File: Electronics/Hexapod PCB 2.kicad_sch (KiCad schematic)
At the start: 68 parts, among them J1 XT60, J2 leg1, J3 leg2, J4 leg3, J5 leg4, J6 leg5, J7 leg6, J8 USB_C_Receptacle_USB2.0_16P, Q1 IRF4905, Q2 Q_NPN_BCE, Q3 Q_NPN_BCE, SW1 SW_SPST, SW2 SW_SPST, SW3 SW_SPST, U1 TPS563201, U2 TPS563201, U3 ESP32-S3-WROOM-1, U4 USBLC6-2P6, U5 BNO055, U6 INA226

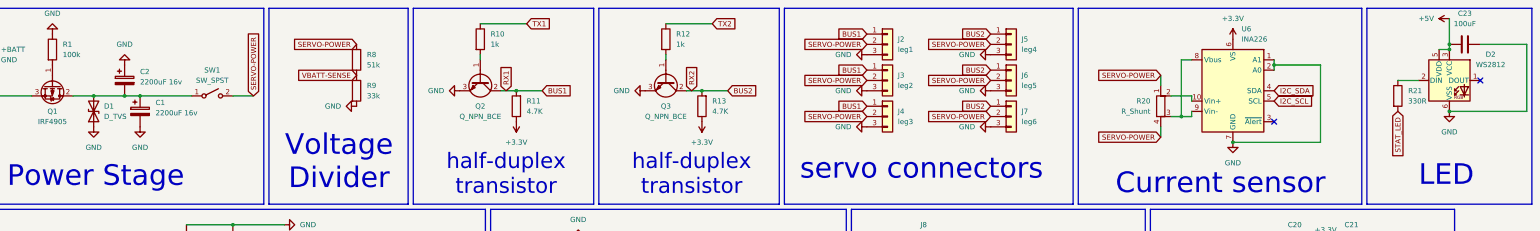
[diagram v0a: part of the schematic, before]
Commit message: finished the schmeatics by redesigning the INA226 , set all of the footprint for the schematics
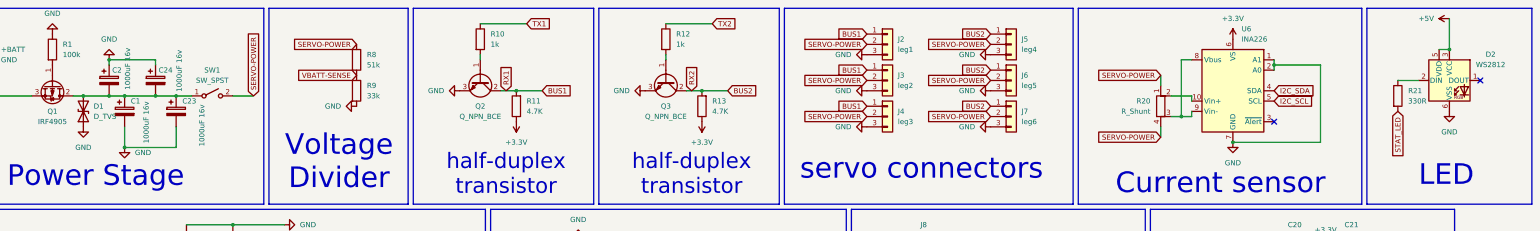
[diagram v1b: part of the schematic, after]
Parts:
- removed C23: 100uF, symbol Device:C
- added C23, C24: 1000uF 16v, Capacitor_SMD:CP_Elec_10x10, symbol Device:C_Polarized
- C1, C2: value 2200uF 16v -> 1000uF 16v; footprint (none) -> Capacitor_SMD:CP_Elec_10x10
- C10, C11, C12, C13, C14, C15, C16, C17, C18, C19, C20, C21, C22, C3, C4, C5, C6, C7, C8, C9: footprint (none) -> Capacitor_SMD:C_0805_2012Metric
- D1: footprint (none) -> Diode_SMD:D_SMB
- J1: footprint (none) -> Connector_AMASS:AMASS_XT60PW-M_1x02_P7.20mm_Horizontal
- J2, J3, J4, J5, J6, J7: footprint (none) -> Connector_JST:JST_PH_B3B-PH-K_1x03_P2.00mm_Vertical
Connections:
- net GND: now also C23.2, C24.1
- net at C1.1, C2.2, D1.2 (A2)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: now also C23.1, C24.2
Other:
- moved on the sheet: C1, C2, D1

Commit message: first version of placement of the components on the pcb is finished also corrected the footprints and schematics
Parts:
- removed R20: R_Shunt, symbol Device:R_Shunt
- removed SW1: SW_SPST, symbol Switch:SW_SPST
- added C25: 0.1uF, Capacitor_SMD:C_0805_2012Metric, symbol Device:C
- added H1, H2, H3, H4: MountingHole, MountingHole:MountingHole_3.2mm_M3, symbol Mechanical:MountingHole
- added R20, R22, R23, R24: 10k, Resistor_SMD:R_0805_2012Metric, symbol Device:R
- added R25, R26: 4.7k, Resistor_SMD:R_0805_2012Metric, symbol Device:R
- added R27: RS, Resistor_SMD:R_2512_6332Metric, symbol Device:R
- J8: footprint (none) -> Connector_USB:USB_C_Receptacle_HRO_TYPE-C-31-M-12
- L1, L2: footprint (none) -> Inductor_SMD:L_Bourns-SRN4018
- Q1: footprint Package_TO_SOT_THT:TO-220-3_Vertical -> Package_TO_SOT_SMD:TO-263-2
- Q2, Q3: footprint (none) -> Package_TO_SOT_SMD:SOT-23
- R1, R10, R11, R12, R13, R14, R15, R16, R17, R18, R19, R2, R21, R3, R4, R5, R6, R7, R8, R9: footprint (none) -> Resistor_SMD:R_0805_2012Metric
- SW2, SW3: footprint (none) -> Button_Switch_SMD:SW_SPST_TS-1088-xR020
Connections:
- net +3.3V: now also C12.2, C13.2, L2.2, C25.2, R23.1, R24.1, R25.2, R26.1
- net +5V: no longer C12.2, C13.2, L2.2
- net GND: now also C2.2, C24.2, C25.1, R20.2, R22.2; no longer C2.1, C24.1, U6.1 (A1), U6.2 (A0)
- net I2C_SCL: now also R25.1
- net I2C_SDA: now also R26.2
- net SERVO-POWER: now also C1.1, C2.1, C23.1, C24.1, D1.2 (A2), Q1.2 (D), U6.10 (Vin+), U6.8 (Vbus), U6.9 (Vin-), R27.1, R27.2
- new net: R22.1, R24.2, U6.2 (A0)
- new net: R20.1, R23.2, U6.1 (A1)
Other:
- moved on the sheet: C1, C10, C11, C12, C13, C14, C15, C16, C17, C18, C19, C2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
